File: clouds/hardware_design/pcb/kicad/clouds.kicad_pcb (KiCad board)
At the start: 2 copper layers, 88.9 x 106 mm, 150 parts, among them IC1 74595D, IC10 TL072D, IC2 LM1117-3.3, IC3 MCP6002, IC4 MCP6004, IC5 STM32F405RGT6, IC6 LM4040B10, IC7 LM1117-3.3, IC8 WM8731, IC9 TL072D, J1 PJ301_THONKICONN6, J10 PJ301_THONKICONN6, J11 PJ301_THONKICONN6, J12 PJ301_THONKICONN6, J2 PJ301_THONKICONN6, J3 PJ301_THONKICONN6, J4 PJ301_THONKICONN6, J5 PJ301_THONKICONN6, J6 PJ301_THONKICONN6, J7 PJ301_THONKICONN6, J8 PJ301_THONKICONN6, J9 PJ301_THONKICONN6, Q1 MMBT3904, Q2 MMBT3904, Q3 8MHz, Q4 12.288MHz, SW1 SW_Push_LED, SW2 TAC_SWITCHPTH, SW3 TAC_SWITCHPTH, SW4 EVQQ2, SW5 EVQQ2

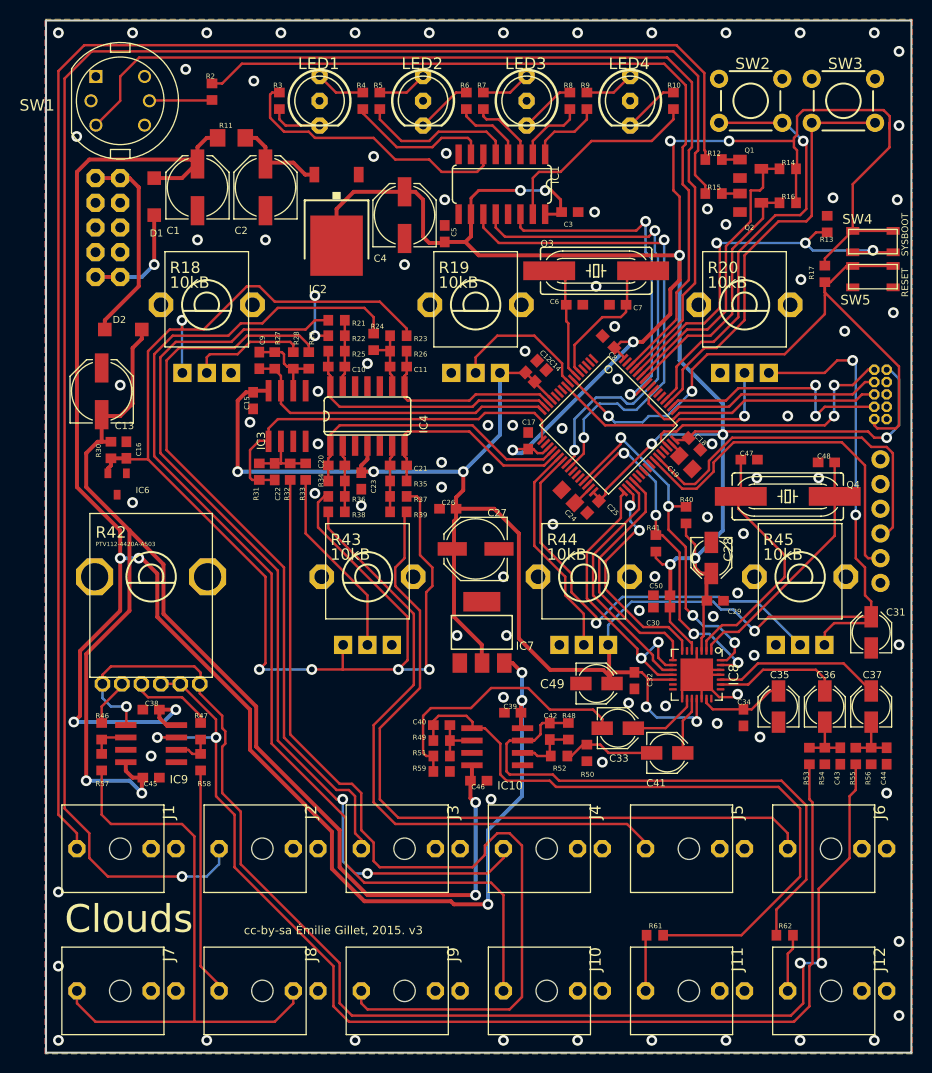
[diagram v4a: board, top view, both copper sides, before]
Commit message: clouds: thonk/alpha dual gang pot
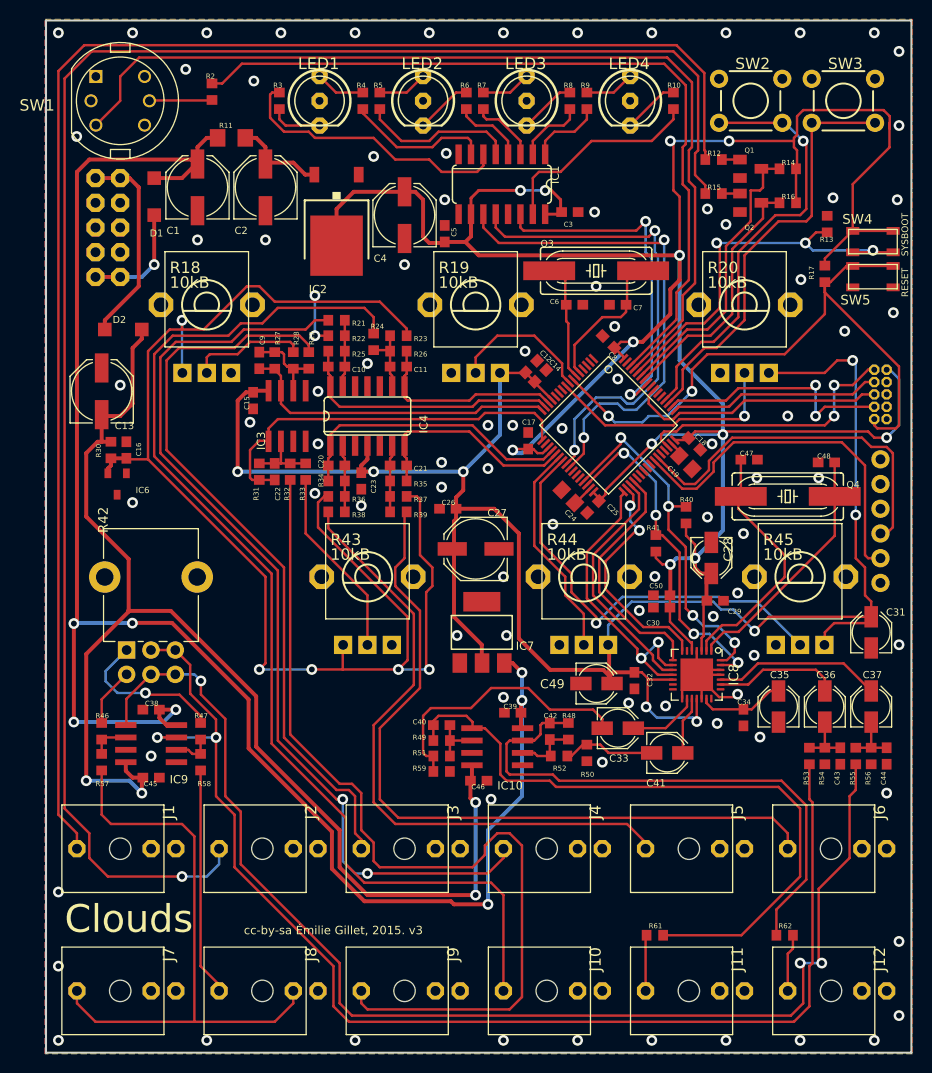
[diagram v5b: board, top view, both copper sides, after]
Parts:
- R42: value PTV112-4420A-A503 -> R_Potentiometer_Dual_Separate; footprint clouds:BOURNS_PTV112 -> Potentiometer_THT:Potentiometer_Alpha_RD902F-40-00D_Dual_Vertical_CircularHoles
- turned R42 to 90 degrees
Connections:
- R42 pad 1: Net-(R42-Pad1) -> Net-(R47-Pad1)
- R42 pad 2: Net-(IC9-Pad1) -> Net-(IC9-Pad7)
- R42 pad 3: Net-(IC9-Pad1) -> Net-(IC9-Pad7)
- R46 pad 1: Net-(R42-Pad1) -> Net-(R46-Pad1)
- R47 pad 1: Net-(R42-Pad1P) -> Net-(R47-Pad1)
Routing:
- net Net-(R47-Pad1): track 0.00 -> 16.2 mm, vias 0 -> 1
- net Net-(R42-Pad1P): track 8.52 -> 0.00 mm
- net Net-(IC9-Pad1): track 135.2 -> 127.9 mm
- net Net-(R46-Pad1): track 0.00 -> 6.06 mm
- net VEE: track 137.5 -> 131.9 mm
- net Net-(R42-Pad1): track 4.63 -> 0.00 mm
- net Net-(IC9-Pad7): track 125.0 -> 129.2 mm
- net VCC: track 188.5 -> 184.3 mm
- net +3V3_A: track 204.9 -> 204.4 mm
